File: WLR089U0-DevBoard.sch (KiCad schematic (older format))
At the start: 23 parts, among them IC1 WLR089U0-I_RM, J1 USB_B_Micro, J2 Conn_ARM_JTAG_SWD_10, J3 Conn_01x10_Female, J4 Conn_01x02_Male, J5 Conn_01x10_Female, J6 Conn_01x10_Male, SW1 SW_Push, U1 MCP1700-3302E_SOT23, U2 CH304E

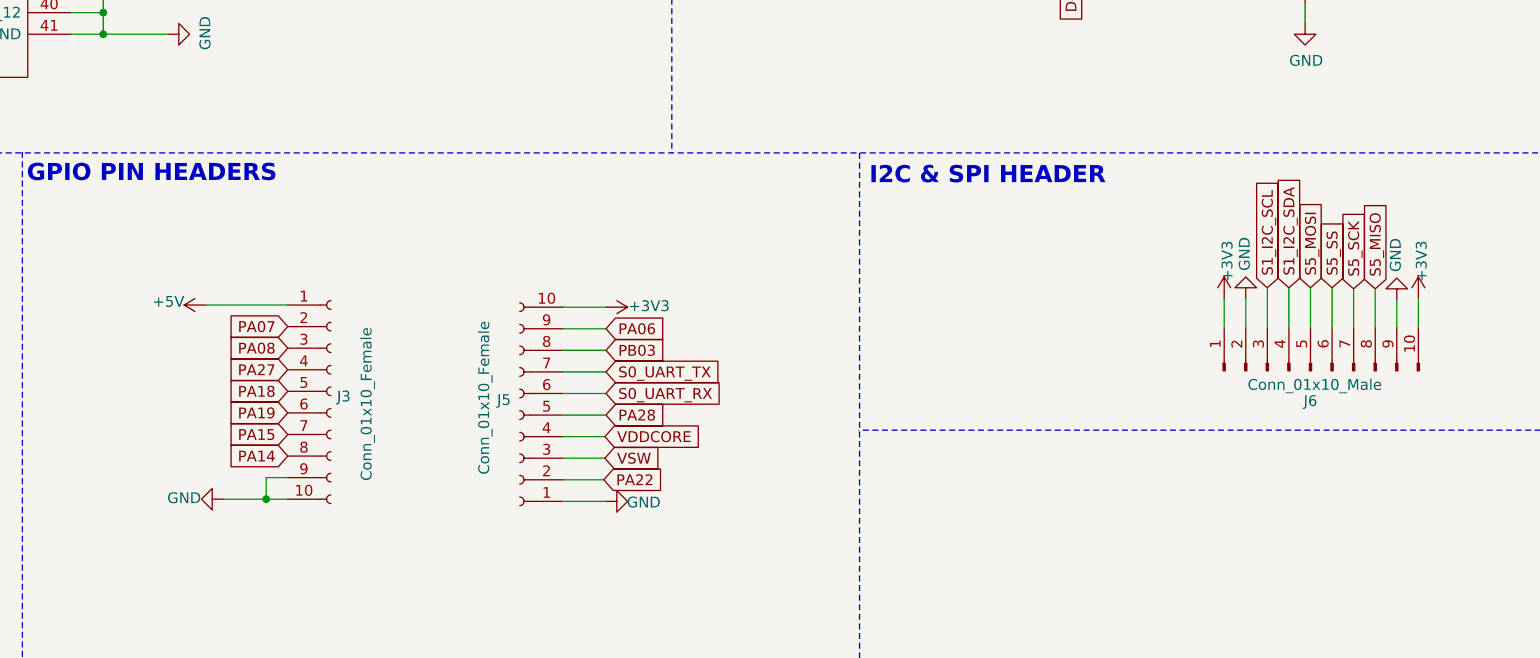
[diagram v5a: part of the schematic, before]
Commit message: placement of ic2 done
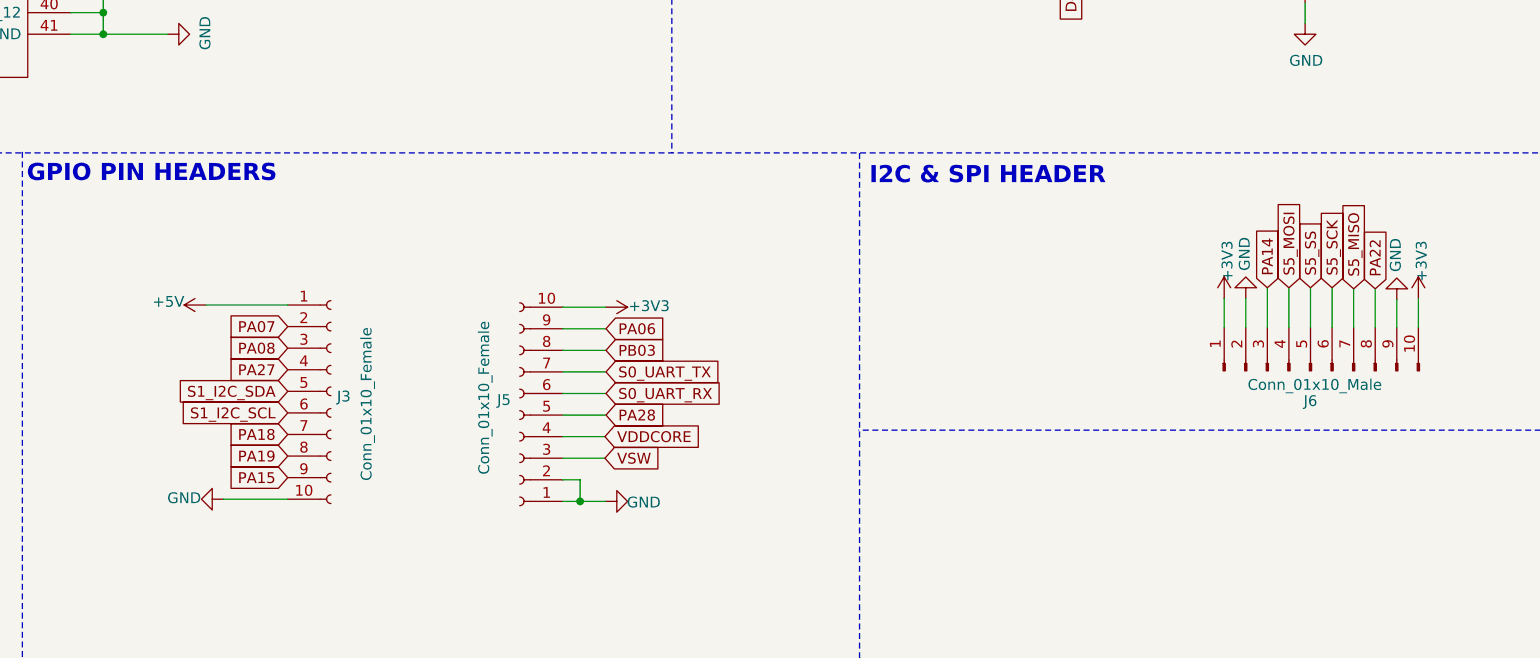
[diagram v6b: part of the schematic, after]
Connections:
- net GND: now also J5.2 (Pin_2); no longer J3.9 (Pin_9)
- net PA14: now also J6.3 (Pin_3); no longer J3.8 (Pin_8)
- net PA15: now also J3.9 (Pin_9); no longer J3.7 (Pin_7)
- net PA18: now also J3.7 (Pin_7); no longer J3.5 (Pin_5)
- net PA19: now also J3.8 (Pin_8); no longer J3.6 (Pin_6)
- net PA22: now also J6.8 (Pin_8); no longer J5.2 (Pin_2)
- net S1_I2C_SCL: now also J3.6 (Pin_6); no longer J6.3 (Pin_3)
- net S1_I2C_SDA: now also J3.5 (Pin_5); no longer J6.4 (Pin_4)
- net S5_MISO: now also J6.7 (Pin_7); no longer J6.8 (Pin_8)
- net S5_MOSI: now also J6.4 (Pin_4); no longer J6.5 (Pin_5)
- net S5_SCK: now also J6.6 (Pin_6); no longer J6.7 (Pin_7)
- net S5_SS: now also J6.5 (Pin_5); no longer J6.6 (Pin_6)
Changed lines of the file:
@@
 EESchema Schematic File Version 4
+LIBS:WLR089U0-DevBoard-cache
 EELAYER 30 0
 EELAYER END
@@
 Wire Wire Line
 	8795 5995 8795 5810
+Text GLabel 8895 5810 1    50   Input ~ 0
+S5_MOSI
 Text GLabel 8995 5810 1    50   Input ~ 0
-S5_MOSI
+S5_SS
 Text GLabel 9095 5810 1    50   Input ~ 0
-S5_SS
+S5_SCK
 Text GLabel 9195 5815 1    50   Input ~ 0
-S5_SCK
-Text GLabel 9295 5815 1    50   Input ~ 0
 S5_MISO
 $Comp
@@
 	0    -1   -1   0
 $EndComp
-Text GLabel 8895 5810 1    50   Input ~ 0
+Text GLabel 4255 6290 0    50   Input ~ 0
 S1_I2C_SDA
 $Comp
@@
 	-1   0    0    1
 $EndComp
-Text GLabel 8795 5810 1    50   Input ~ 0
+Text GLabel 4255 6390 0    50   Input ~ 0
 S1_I2C_SCL
 Wire Wire Line
@@
 	1    0    0    -1
 $EndComp
-Wire Wire Line
-	3955 6790 4155 6790
 Wire Notes Line
 	11130 6470 6900 6470
@@
 	5530 6400 5730 6400
 Wire Wire Line
-	5530 6800 5730 6800
+	5530 6800 5610 6800
 $Comp
 L power:GND #PWR021
@@
 Text GLabel 5730 6000 2    50   Input ~ 0
 PA06
-Text GLabel 5720 6700 2    50   Input ~ 0
+Text GLabel 9295 5815 1    50   Input ~ 0
 PA22
+Text GLabel 8795 5810 1    50   Input ~ 0
+PA14
+Text GLabel 4255 6690 0    50   Input ~ 0
+PA15
 Text GLabel 4255 6590 0    50   Input ~ 0
-PA14
+PA19
 Text GLabel 4255 6490 0    50   Input ~ 0
-PA15
-Text GLabel 4255 6390 0    50   Input ~ 0
-PA19
-Text GLabel 4255 6290 0    50   Input ~ 0
 PA18
 Text GLabel 4255 6190 0    50   Input ~ 0
@@
 S0_UART_TX
 Wire Wire Line
-	4155 6790 4155 6690
-Wire Wire Line
-	4155 6690 4255 6690
-Connection ~ 4155 6790
-Wire Wire Line
-	4155 6790 4255 6790
-Wire Wire Line
-	5530 6700 5720 6700
-Wire Wire Line
 	5530 6600 5725 6600
 Wire Wire Line
@@
 Wire Wire Line
 	3875 5890 4255 5890
+Wire Wire Line
+	3955 6790 4255 6790
+Wire Wire Line
+	5530 6700 5610 6700
+Wire Wire Line
+	5610 6700 5610 6800
+Connection ~ 5610 6800
+Wire Wire Line
+	5610 6800 5730 6800
 $EndSCHEMATC

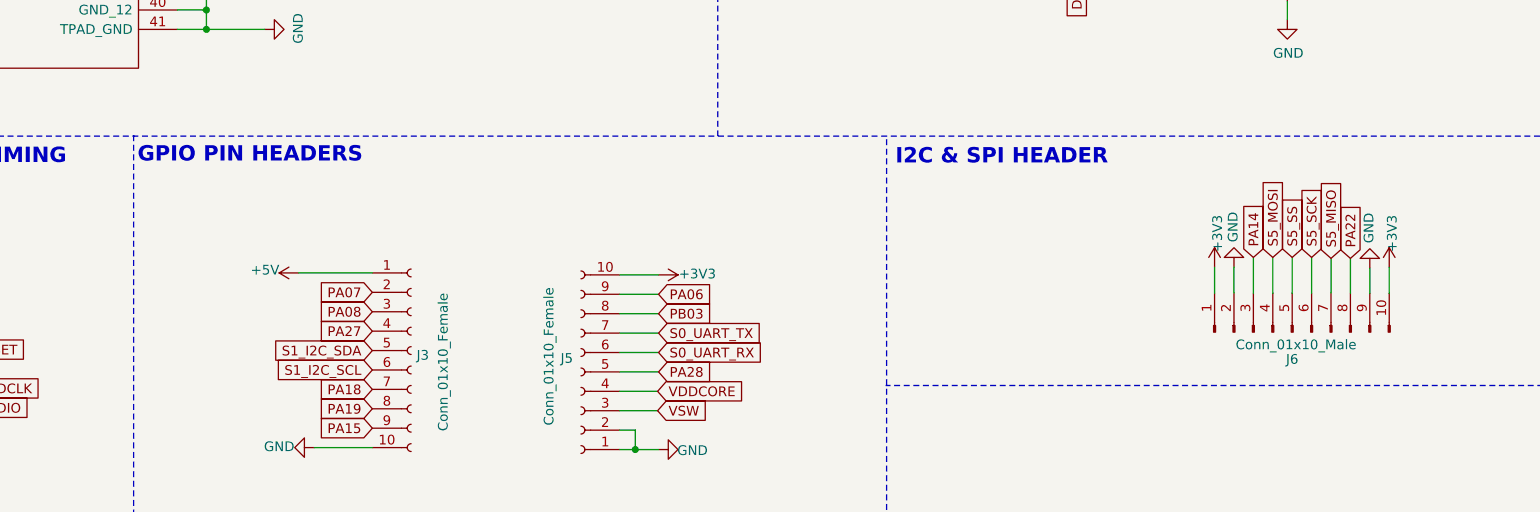
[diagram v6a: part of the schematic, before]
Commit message: updated pin header to 8 pin, updated layout
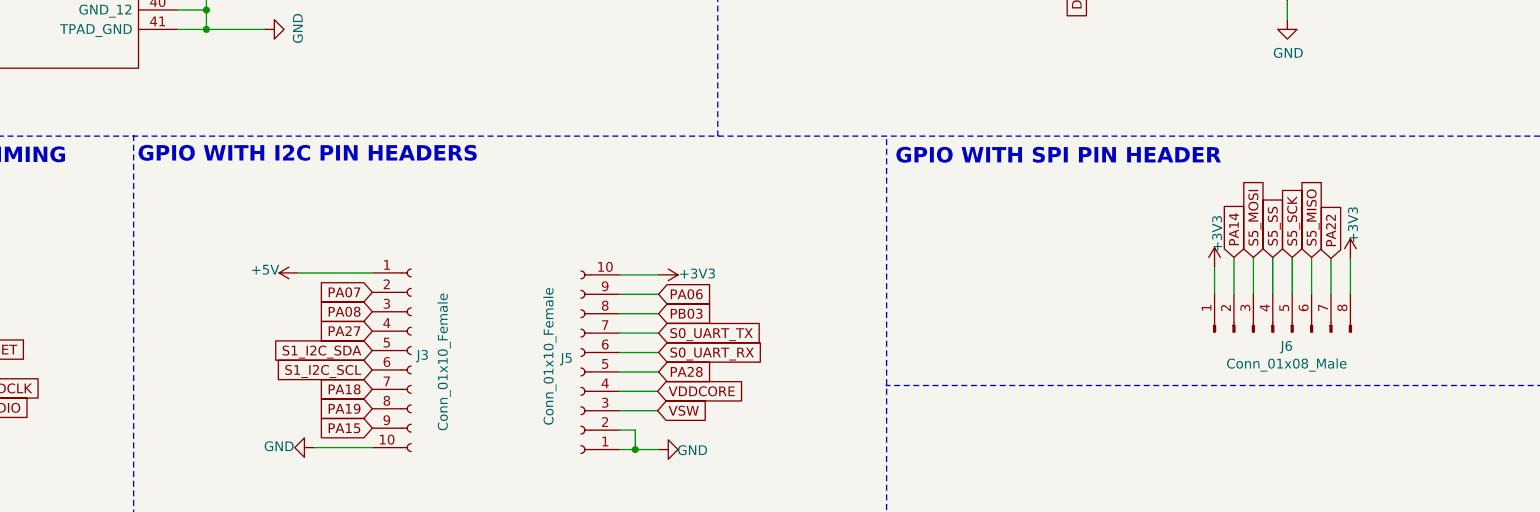
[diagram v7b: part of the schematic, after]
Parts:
- removed J6: Conn_01x10_Male, Connector_PinHeader_2.54mm:PinHeader_1x10_P2.54mm_Vertical, symbol Connector:Conn_01x10_Male
- added J6: Conn_01x08_Male, Connector_PinHeader_2.54mm:PinHeader_1x08_P2.54mm_Vertical, symbol Connector:Conn_01x08_Male
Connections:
- net +3V3: now also J6.1 (Pin_1), J6.8 (Pin_8)
- net PA14: now also J6.2 (Pin_2)
- net PA22: now also J6.7 (Pin_7)
- net S5_MISO: now also J6.6 (Pin_6)
- net S5_MOSI: now also J6.3 (Pin_3)
- net S5_SCK: now also J6.5 (Pin_5)
- net S5_SS: now also J6.4 (Pin_4)
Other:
- note added: "GPIO WITH I2C PIN HEADERS"
- note added: "GPIO WITH SPI PIN HEADER"
- note removed: "GPIO PIN HEADERS"
- note removed: "I2C & SPI HEADER"
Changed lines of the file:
@@
 EESchema Schematic File Version 4
-LIBS:WLR089U0-DevBoard-cache
 EELAYER 30 0
 EELAYER END
@@
 	6035 555  6035 5185
 Text Notes 3045 5330 0    79   ~ 16
-GPIO PIN HEADERS
+GPIO WITH I2C PIN HEADERS
 NoConn ~ 2150 6785
 NoConn ~ 2150 6685
@@
 	8325 2830 8325 3045
 Text Notes 6950 5340 0    79   ~ 16
-I2C & SPI HEADER
-Wire Wire Line
-	9495 5995 9495 5860
-Wire Wire Line
-	9395 5995 9395 5865
+GPIO WITH SPI PIN HEADER
 $Comp
 L power:+3V3 #PWR031
 U 1 1 601BFB9C
-P 9495 5860
-F 0 "#PWR031" H 9495 5710 50  0001 C CNN
-F 1 "+3V3" V 9510 6033 50  0000 C CNN
-F 2 "" H 9495 5860 50  0001 C CNN
-F 3 "" H 9495 5860 50  0001 C CNN
-	1    9495 5860
+P 9295 5815
+F 0 "#PWR031" H 9295 5665 50  0001 C CNN
+F 1 "+3V3" V 9310 5988 50  0000 C CNN
+F 2 "" H 9295 5815 50  0001 C CNN
+F 3 "" H 9295 5815 50  0001 C CNN
+	1    9295 5815
 	1    0    0    -1
 $EndComp
@@
 $EndComp
 Wire Wire Line
-	8695 5995 8695 5860
-$Comp
-L power:GND #PWR027
-U 1 1 601BC218
-P 8695 5860
-F 0 "#PWR027" H 8695 5610 50  0001 C CNN
-F 1 "GND" V 8700 5732 50  0000 R CNN
-F 2 "" H 8695 5860 50  0001 C CNN
-F 3 "" H 8695 5860 50  0001 C CNN
-	1    8695 5860
-	-1   0    0    1
-$EndComp
+	8695 5995 8695 5810
 Wire Wire Line
 	9295 5995 9295 5815
@@
 Wire Wire Line
 	8795 5995 8795 5810
+Text GLabel 8795 5810 1    50   Input ~ 0
+S5_MOSI
 Text GLabel 8895 5810 1    50   Input ~ 0
-S5_MOSI
+S5_SS
 Text GLabel 8995 5810 1    50   Input ~ 0
-S5_SS
+S5_SCK
 Text GLabel 9095 5810 1    50   Input ~ 0
-S5_SCK
-Text GLabel 9195 5815 1    50   Input ~ 0
 S5_MISO
-$Comp
-L Connector:Conn_01x10_Male J6
-U 1 1 6031E5B3
-P 8995 6195
-F 0 "J6" V 8855 6195 50  0000 C CNN
-F 1 "Conn_01x10_Male" V 8930 6175 50  0000 C CNN
-F 2 "Connector_PinHeader_2.54mm:PinHeader_1x10_P2.54mm_Vertical" H 8995 6195 50  0001 C CNN
-F 3 "~" H 8995 6195 50  0001 C CNN
-	1    8995 6195
-	0    -1   -1   0
-$EndComp
 Text GLabel 4255 6290 0    50   Input ~ 0
 S1_I2C_SDA
-$Comp
-L power:GND #PWR029
-U 1 1 602FCC79
-P 9395 5865
-F 0 "#PWR029" H 9395 5615 50  0001 C CNN
-F 1 "GND" V 9400 5737 50  0000 R CNN
-F 2 "" H 9395 5865 50  0001 C CNN
-F 3 "" H 9395 5865 50  0001 C CNN
-	1    9395 5865
-	-1   0    0    1
-$EndComp
 Text GLabel 4255 6390 0    50   Input ~ 0
 S1_I2C_SCL
@@
 Text GLabel 5730 6000 2    50   Input ~ 0
 PA06
-Text GLabel 9295 5815 1    50   Input ~ 0
+Text GLabel 9195 5815 1    50   Input ~ 0
 PA22
-Text GLabel 8795 5810 1    50   Input ~ 0
+Text GLabel 8695 5810 1    50   Input ~ 0
 PA14
 Text GLabel 4255 6690 0    50   Input ~ 0
@@
 Wire Wire Line
 	5610 6800 5730 6800
+$Comp
+L Connector:Conn_01x08_Male J6
+U 1 1 602487A1
+P 8895 6195
+F 0 "J6" V 8822 6123 50  0000 C CNN
+F 1 "Conn_01x08_Male" V 8731 6123 50  0000 C CNN
+F 2 "Connector_PinHeader_2.54mm:PinHeader_1x08_P2.54mm_Vertical" H 8895 6195 50  0001 C CNN
+F 3 "~" H 8895 6195 50  0001 C CNN
+	1    8895 6195
+	0    -1   -1   0
+$EndComp
 $EndSCHEMATC

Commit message: editing
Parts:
- added C4, C5: 100n, Capacitor_SMD:C_0402_1005Metric_Pad0.74x0.62mm_HandSolder, symbol Device:C_Small
- added R4, R5: 4.7k, Resistor_SMD:R_1206_3216Metric_Pad1.42x1.75mm_HandSolder, symbol Device:R_Small
- C3: footprint Capacitor_SMD:C_1206_3216Metric_Pad1.33x1.80mm_HandSolder -> Capacitor_SMD:C_0402_1005Metric_Pad0.74x0.62mm_HandSolder
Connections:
- net +3V3: now also C4.1, C5.1, R4.1, R5.1
- net GND: now also C4.2, C5.2
- net S1_I2C_SCL: now also R5.2
- net S1_I2C_SDA: now also R4.2
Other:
- moved on the sheet: IC1
